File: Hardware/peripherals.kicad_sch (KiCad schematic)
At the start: 0 parts

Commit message: feat: implement system peripherals (OSD, Gyro, Baro)
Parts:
- added C22, C23, C24, C25, C26, C27, C30: 100nF 16V, symbol Device:C
- added C28, C29: 22pF 16V, symbol Device:C
- added C31: 47uF 16V, symbol Device:C_Polarized
- added R7, R8: 4.7k, symbol Device:R
- added U5: BMI270, BMI270:XDCR_BMI270, symbol BMI270:BMI270
- added U6: DPS310, DPS310:XDCR_DPS310, symbol DPS310:DPS310
- added U7: MAX7456EUI_T, Package_SO:TSSOP-28-1EP_4.4x9.7mm_P0.65mm_EP2.74x4.75mm, symbol MAX7456EUI_T:MAX7456EUI_T
- added Y2: Crystal, symbol Device:Crystal
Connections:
- new net: C30.1, U7.22 (VIN)
- new net: C31.1, U7.26 (VOUT)
- new net: C28.1, U7.5 (CLKIN), Y2.2
- new net: C29.1, U7.6 (XFB), Y2.1
- new net +3.3V: C22.2, C23.2, C24.1, R7.1, R8.2, U5.5 (VDDIO), U5.8 (VDD), U6.2 (~{CSB}), U6.6 (VDDIO), U6.8 (VDD)
- new net +5V: C25.1, C26.1, C27.1, U7.19 (~{RESET}), U7.21 (AVDD), U7.24 (PVDD), U7.3 (DVDD)
- new net CAM_VIDEO_IN: C30.2
- new net GND: C22.1, C23.1, C24.2, C25.2, C26.2, C27.2, C28.2, C29.2, U5.6 (GNDIO), U5.7 (GND), U6.1 (GND), U6.5 (SDO), U6.7 (GND), U7.20 (AGND), U7.23 (PGND), U7.29 (EP), U7.4 (DGND)
- new net GYRO_CS: U5.12 (CSB)
- new net GYRO_EXTI: U5.4 (INT1)
- new net I2C1_SCL: R8.1, U6.4 (SCK)
- new net I2C1_SDA: R7.2, U6.3 (SDI)
- new net OSD_CS: U7.8 (~{CS})
- new net SPI1_MISO: U5.1 (SDO)
- new net SPI1_MOSI: U5.14 (SDX)
- new net SPI1_SCK: U5.13 (SCX)
- new net SPI2_MISO: U7.11 (SDOUT)
- new net SPI2_MOSI: U7.9 (SDIN)
- new net SPI2_SCK: U7.10 (SCLK)
- new net VTX_VIDEO_OUT: C31.2
- no-connect marks 0 -> 10

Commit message: Finalize schematic: Add connectors, LEDs, Buzzer and fix all ERC errors
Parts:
- added D2: Red, symbol Device:D
- added D3: Blue, symbol Device:D
- added Q1: 2N7002, Package_TO_SOT_SMD:SOT-23, symbol Transistor_FET:2N7002
- added R13, R16: 1k, symbol Device:R
- added R14: 10k, symbol Device:R
- added R17: 330Ω, symbol Device:R
- added R18: 4.7k, symbol Device:R
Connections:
- net GND: now also D2.1 (K), D3.1 (K), Q1.2 (S), R14.1, R18.2; no longer U6.5 (SDO)
- net +3.3V renamed +3V3
- net +3V3: now also R16.1
- new net: Q1.1 (G), R13.1, R14.2
- new net: D2.2 (A), R16.2
- new net: D3.2 (A), R17.2
- new net: R18.1, U6.5 (SDO)
- new net BUZZER-: Q1.3 (D)
- new net BUZZER_CTRL: R13.2
- new net LED_STATUS: R17.1
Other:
- note added: "BAROMETER"
- note added: "BUZZER DRIVER"
- note added: "IMU / GYRO"
- note added: "LED_POWER"
- note added: "LED_STATUS"
- note added: "OSD (ON-SCREEN DISPLAY)"

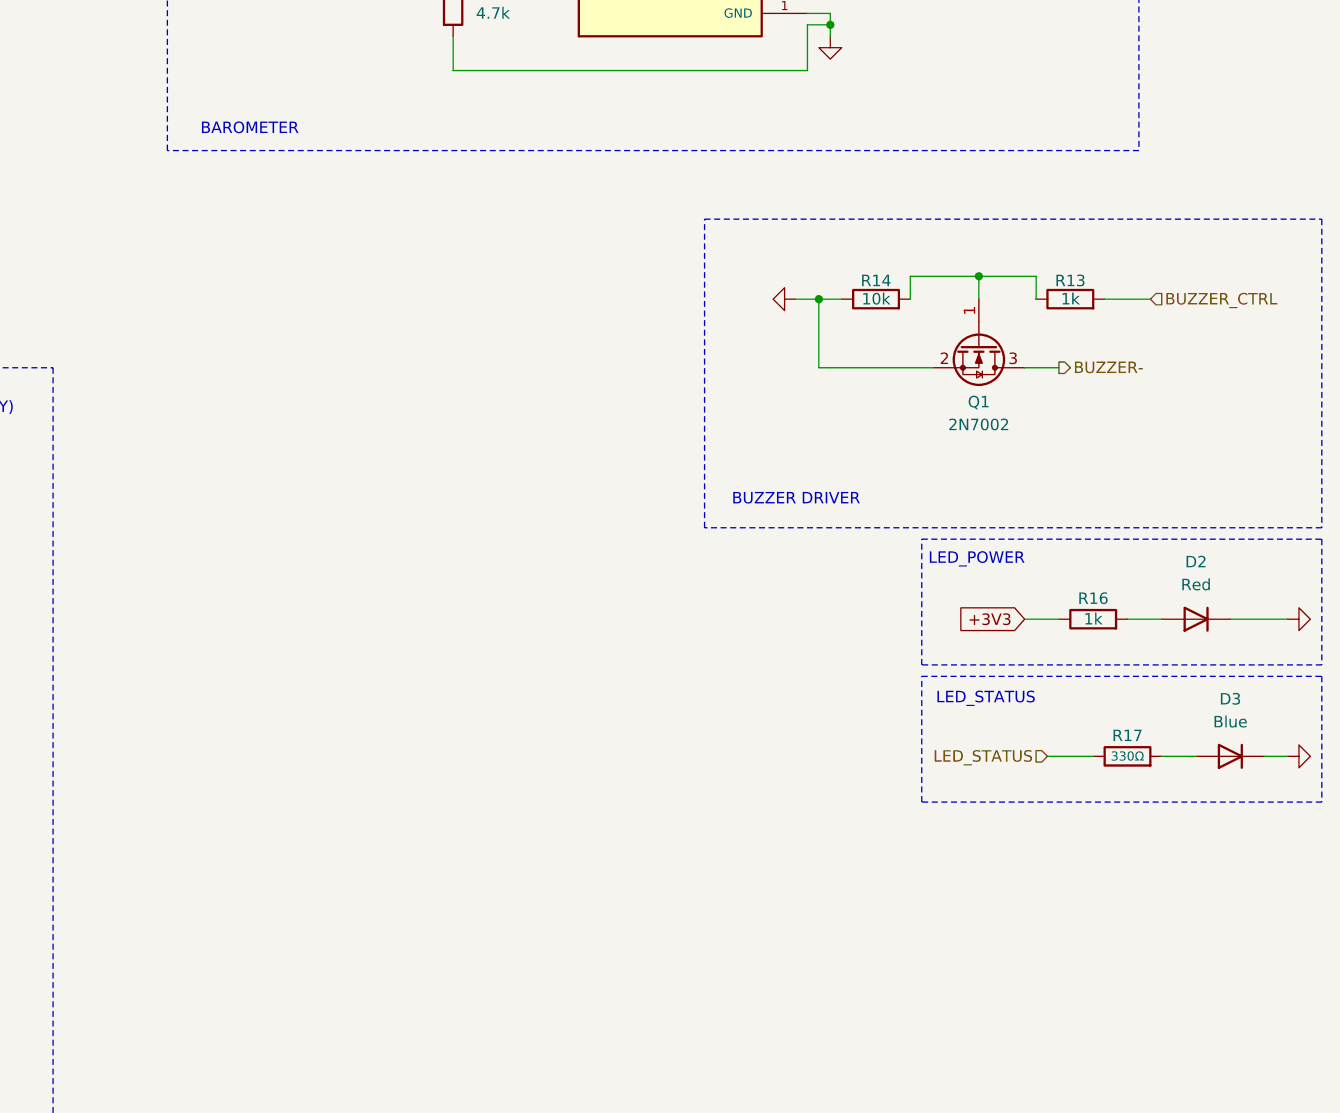
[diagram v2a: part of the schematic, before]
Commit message: Update schematic: Add SDIO Blackbox, ESC Redundancy and remove UART5
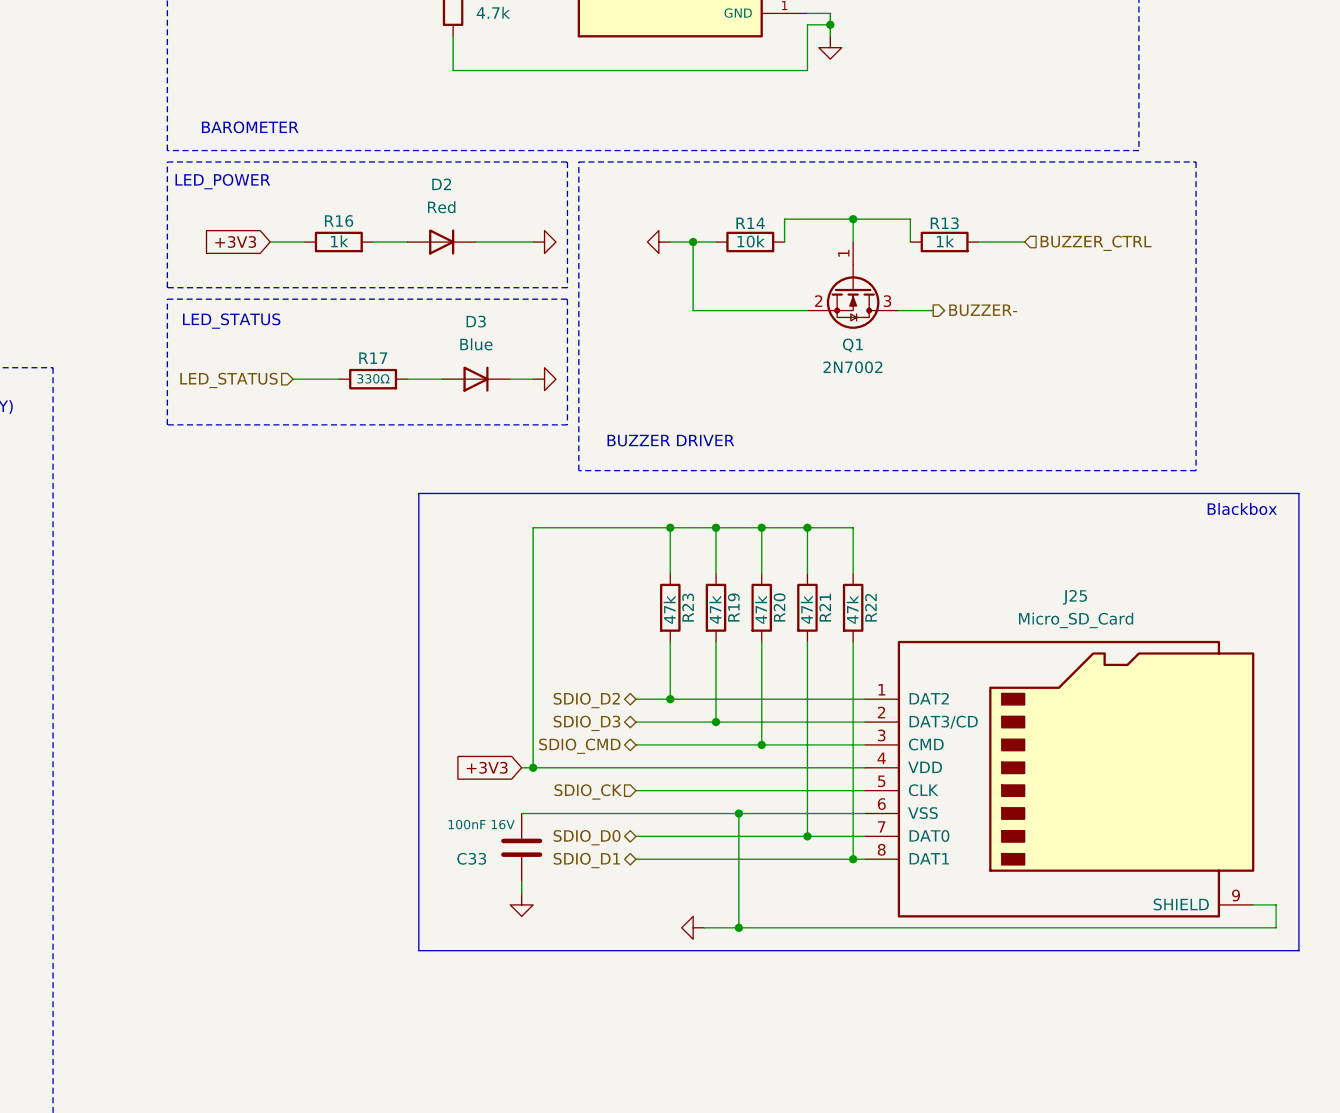
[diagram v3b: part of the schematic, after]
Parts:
- added C33: 100nF 16V, symbol Device:C
- added J25: Micro_SD_Card, symbol Connector:Micro_SD_Card
- added R19, R20, R21, R22, R23: 47k, symbol Device:R
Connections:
- net +3V3: now also J25.4 (VDD), R19.1, R20.1, R21.1, R22.1, R23.1
- net GND: now also C33.1, C33.2, J25.6 (VSS), J25.9 (SHIELD)
- new net SDIO_CK: J25.5 (CLK)
- new net SDIO_CMD: J25.3 (CMD), R20.2
- new net SDIO_D0: J25.7 (DAT0), R21.2
- new net SDIO_D1: J25.8 (DAT1), R22.2
- new net SDIO_D2: J25.1 (DAT2), R23.2
- new net SDIO_D3: J25.2 (DAT3/CD), R19.2
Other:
- note added: "Blackbox"
- moved on the sheet: D2, D3, Q1, R13, R14, R16, R17

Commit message: Finalize component placement and silkscreen
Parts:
- C22, C23, C24, C25, C26, C27, C28, C29, C30, C33: footprint (none) -> Capacitor_SMD:C_0402_1005Metric
- C31: footprint (none) -> Capacitor_SMD:C_0805_2012Metric
- D2, D3: footprint (none) -> LED_SMD:LED_0402_1005Metric
- J25: footprint (none) -> Connector_Card:microSD_HC_Hirose_DM3D-SF
- R13, R14, R16, R17, R18, R19, R20, R21, R22, R23, R7, R8: footprint (none) -> Resistor_SMD:R_0402_1005Metric
- U5: footprint BMI270:XDCR_BMI270 -> Package_LGA:Bosch_LGA-14_3x2.5mm_P0.5mm
- U6: footprint DPS310:XDCR_DPS310 -> Crystal:Crystal_SMD_5032-2Pin_5.0x3.2mm
- Y2: footprint (none) -> Crystal:Crystal_SMD_5032-2Pin_5.0x3.2mm
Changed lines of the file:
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@@
 			)
 		)
-		(property "Footprint" ""
+		(property "Footprint" "Resistor_SMD:R_0402_1005Metric"
 			(at 241.3 84.328 90)
 			(effects
@@
 			)
 		)
-		(property "Footprint" ""
+		(property "Footprint" "Resistor_SMD:R_0402_1005Metric"
 			(at 173.99 84.328 90)
 			(effects
@@
 			)
 		)
-		(property "Footprint" ""
+		(property "Footprint" "Capacitor_SMD:C_0805_2012Metric"
 			(at 102.87 151.4348 0)
 			(effects
@@
 			)
 		)
-		(property "Footprint" ""
+		(property "Footprint" "Resistor_SMD:R_0402_1005Metric"
 			(at 219.202 123.19 90)
 			(effects
@@
 			)
 		)
-		(property "Footprint" "BMI270:XDCR_BMI270"
+		(property "Footprint" "Package_LGA:Bosch_LGA-14_3x2.5mm_P0.5mm"
 			(at 46.99 45.72 0)
 			(effects
@@
 			)
 		)
-		(property "Footprint" ""
+		(property "Footprint" "Resistor_SMD:R_0402_1005Metric"
 			(at 177.8 99.568 90)
 			(effects
@@
 			)
 		)
-		(property "Footprint" ""
+		(property "Footprint" "Capacitor_SMD:C_0402_1005Metric"
 			(at 70.8152 184.15 0)
 			(effects
@@
 			)
 		)
-		(property "Footprint" ""
+		(property "Footprint" "Resistor_SMD:R_0402_1005Metric"
 			(at 219.71 84.328 90)
 			(effects
@@
 			)
 		)
-		(property "Footprint" ""
+		(property "Footprint" "Capacitor_SMD:C_0402_1005Metric"
 			(at 83.5152 139.7 0)
 			(effects
@@
 			)
 		)
-		(property "Footprint" ""
+		(property "Footprint" "Crystal:Crystal_SMD_5032-2Pin_5.0x3.2mm"
 			(at 57.15 172.72 0)
 			(effects
@@
 			)
 		)
-		(property "Footprint" ""
+		(property "Footprint" "Resistor_SMD:R_0402_1005Metric"
 			(at 209.042 123.19 90)
 			(effects
@@
 			)
 		)
-		(property "Footprint" ""
+		(property "Footprint" "Connector_Card:microSD_HC_Hirose_DM3D-SF"
 			(at 284.48 133.35 0)
 			(effects
@@
 			)
 		)
-		(property "Footprint" ""
+		(property "Footprint" "Capacitor_SMD:C_0402_1005Metric"
 			(at 105.1052 139.7 0)
 			(effects
@@
 			)
 		)
-		(property "Footprint" ""
+		(property "Footprint" "Resistor_SMD:R_0402_1005Metric"
 			(at 214.122 123.19 90)
 			(effects
@@
 			)
 		)
-		(property "Footprint" ""
+		(property "Footprint" "Capacitor_SMD:C_0402_1005Metric"
 			(at 40.3352 184.15 0)
 			(effects
@@
 			)
 		)
-		(property "Footprint" ""
+		(property "Footprint" "Resistor_SMD:R_0402_1005Metric"
 			(at 193.548 40.64 90)
 			(effects
@@
 			)
 		)
-		(property "Footprint" ""
+		(property "Footprint" "Capacitor_SMD:C_0402_1005Metric"
 			(at 243.5352 39.37 0)
 			(effects
@@
 			)
 		)
-		(property "Footprint" "DPS310:XDCR_DPS310"
+		(property "Footprint" "Crystal:Crystal_SMD_5032-2Pin_5.0x3.2mm"
 			(at 210.82 46.99 0)
 			(effects
@@
 			)
 		)
-		(property "Footprint" ""
+		(property "Footprint" "LED_SMD:LED_0402_1005Metric"
 			(at 189.23 97.79 0)
 			(effects
@@
 			)
 		)
-		(property "Footprint" ""
+		(property "Footprint" "Resistor_SMD:R_0402_1005Metric"
 			(at 229.362 123.19 90)
 			(effects
@@
 			)
 		)
-		(property "Footprint" ""
+		(property "Footprint" "Capacitor_SMD:C_0402_1005Metric"
 			(at 103.8352 26.67 0)
 			(effects
@@
 			)
 		)
-		(property "Footprint" ""
+		(property "Footprint" "Capacitor_SMD:C_0402_1005Metric"
 			(at 193.3448 146.05 0)
 			(effects
@@
 			)
 		)
-		(property "Footprint" ""
+		(property "Footprint" "LED_SMD:LED_0402_1005Metric"
 			(at 185.42 82.55 0)
 			(effects
@@
 			)
 		)
-		(property "Footprint" ""
+		(property "Footprint" "Capacitor_SMD:C_0402_1005Metric"
 			(at 93.6752 139.7 0)
 			(effects
@@
 			)
 		)
-		(property "Footprint" ""
+		(property "Footprint" "Capacitor_SMD:C_0402_1005Metric"
 			(at 93.6752 26.67 0)
 			(effects
@@
 			)
 		)
-		(property "Footprint" ""
+		(property "Footprint" "Capacitor_SMD:C_0402_1005Metric"
 			(at 22.86 149.5552 0)
 			(effects
@@
 			)
 		)
-		(property "Footprint" ""
+		(property "Footprint" "Resistor_SMD:R_0402_1005Metric"
 			(at 184.912 55.88 90)
 			(effects
@@
 			)
 		)
-		(property "Footprint" ""
+		(property "Footprint" "Resistor_SMD:R_0402_1005Metric"
 			(at 173.482 43.18 90)
 			(effects
@@
 			)
 		)
-		(property "Footprint" ""
+		(property "Footprint" "Resistor_SMD:R_0402_1005Metric"
 			(at 224.282 123.19 90)
 			(effects
